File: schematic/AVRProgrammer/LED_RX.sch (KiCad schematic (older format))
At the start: 2 parts

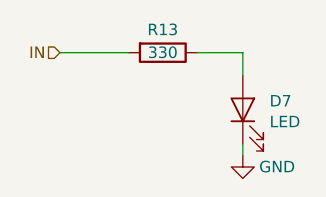
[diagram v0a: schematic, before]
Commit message: 3dmodels for PCB components was added
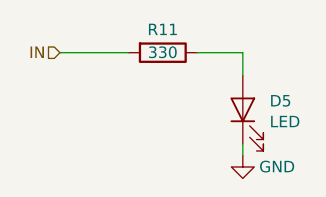
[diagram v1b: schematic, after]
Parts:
- D1: footprint LED_THT:LED_D3.0mm -> LED_THT:LED_D3.0mm_Horizontal_O6.35mm_Z6.0mm
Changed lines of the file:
@@
 $Descr A4 11693 8268
 encoding utf-8
-Sheet 8 8
+Sheet 6 8
 Title ""
 Date ""
@@
 AR Path="/5CA01110/5C9E09EC" Ref="D6"  Part="1"
 AR Path="/5CA084E5/5C9E09EC" Ref="D7"  Part="1"
-F 0 "D7" V 5588 3583 50  0000 R CNN
+F 0 "D5" V 5588 3583 50  0000 R CNN
 F 1 "LED" V 5497 3583 50  0000 R CNN
-F 2 "LED_THT:LED_D3.0mm" H 5550 3700 50  0001 C CNN
+F 2 "LED_THT:LED_D3.0mm_Horizontal_O6.35mm_Z6.0mm" H 5550 3700 50  0001 C CNN
 F 3 "" H 5550 3700 50  0001 C CNN
 	1    5550 3700
@@
 AR Path="/5CA01110/5C9E09F3" Ref="#PWR026"  Part="1"
 AR Path="/5CA084E5/5C9E09F3" Ref="#PWR027"  Part="1"
-F 0 "#PWR027" H 5550 3650 50  0001 C CNN
+F 0 "#PWR025" H 5550 3650 50  0001 C CNN
 F 1 "GND" H 5700 3850 50  0000 C CNN
 F 2 "" H 5550 3900 50  0001 C CNN
@@
 AR Path="/5CA01110/5C9E09FB" Ref="R12"  Part="1"
 AR Path="/5CA084E5/5C9E09FB" Ref="R13"  Part="1"
-F 0 "R13" V 5100 3450 50  0000 C CNN
+F 0 "R11" V 5100 3450 50  0000 C CNN
 F 1 "330" V 5200 3450 50  0000 C CNN
 F 2 "Resistor_SMD:R_0805_2012Metric" V 5130 3450 50  0001 C CNN
